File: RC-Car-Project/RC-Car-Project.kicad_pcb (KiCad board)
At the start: 2 copper layers, 80 x 120 mm, 118 parts, among them J1 Conn_01x02_Pin, J10 Conn_01x02, J2 Conn_01x02_Pin, J3 Conn_01x02_Pin, J4 Conn_01x02_Pin, J5 MCU_IF, J6 ANT_IF, J7 Conn_02x09_Odd_Even, J8 Conn_01x02, J9 Conn_01x02, Q1 BTN8982TA, Q2 BTN8982TA, Q3 2N7002E, Q4 2N7002E, Q5 BTN8982TA, Q6 BTN8982TA, Q7 2N7002E, SW1 SW_Push, U1 AT86RF215-ZU, U2 A6986F3V3TR, U3 ADC082S021CIMM/NOPB, U4 LMR16020PDDAR, U5 RFX2401C, U6 2450FB15A050E, U7 STM32H743VGTx, U8 INA229AQDGSRQ1, U9 SN74HC244PWR, Y1 Crystal

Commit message: Moved stuff around
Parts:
- moved SW1 75.9 mm to (59.1, 132.0)
- moved C10 75.9 mm to (74.9, 132.9)
- moved C11 75.9 mm to (74.9, 134.6)
- moved C14 75.9 mm to (86.1, 114.6)
- moved C15 75.9 mm to (86.1, 118.9)
- moved C2 75.9 mm to (86.1, 110.4)
- moved C22 75.9 mm to (92.6, 109.1)
- moved C23 75.9 mm to (92.6, 110.9)
- moved C37 75.9 mm to (92.6, 112.6)
- moved C39 75.9 mm to (86.1, 123.1)
- moved C43 75.9 mm to (92.6, 114.4)
- moved C44 75.9 mm to (92.6, 116.1)
- moved C45 75.9 mm to (92.6, 117.9)
- moved C46 75.9 mm to (86.1, 127.4)
- moved C47 75.9 mm to (86.1, 131.6)
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
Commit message: Candidate for layout #1?
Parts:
- moved U3 134.2 mm to (175.5, 116.0)
- moved Q4 126.9 mm to (172.9, 123.5)
- moved Q7 126.2 mm to (173.0, 136.5)
- moved Q3 126.1 mm to (173.0, 130.0)
- moved U1 105.8 mm to (138.5, 132.0)
- moved J6 101.4 mm to (116.2, 130.9)
- moved R15 98.3 mm to (129.0, 92.5)
- moved U6 96.9 mm to (131.9, 131.0)
- moved U5 94.9 mm to (124.5, 130.5), turned to 180 degrees
- moved U8 93.3 mm to (122.0, 96.5), turned to 90 degrees
- moved U7 90.4 mm to (155.5, 132.5), turned to -90 degrees
- moved L2 88.5 mm to (184.0, 108.0), turned to -90 degrees
- moved L1 83.5 mm to (171.5, 97.5), turned to 90 degrees
- moved Y1 81.0 mm to (156.0, 118.0)
- moved J9 80.3 mm to (183.5, 143.8), turned to 90 degrees
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
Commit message: Fixed Drivers
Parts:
- added R32: 10k, Resistor_SMD:R_0201_0603Metric, F.Cu at (93.2, 77.2)
- added R33: 10k, Resistor_SMD:R_0201_0603Metric, F.Cu at (93.2, 79.0)
- added R34: 10k, Resistor_SMD:R_0201_0603Metric, F.Cu at (93.2, 80.8)
- added R35: 10k, Resistor_SMD:R_0201_0603Metric, F.Cu at (93.2, 82.5)
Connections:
- J8 pad 1: /Connectors/LIGHTS1_POS -> +12V
- J9 pad 1: /Connectors/LIGHTS2_POS -> +12V
- Q1 pad 3: Net-(Q1-INH) -> +3V3
- Q2 pad 3: Net-(Q2-INH) -> +3V3
- Q3 pad 3: /MiscDriver/LIGHTS1_NEG -> /Connectors/LIGHTS1_NEG
- Q5 pad 3: Net-(Q5-INH) -> +3V3
- Q6 pad 3: Net-(Q6-INH) -> +3V3
- Q7 pad 3: /MiscDriver/LIGHTS2_NEG -> /Connectors/LIGHTS2_NEG
- R1 pad 1: /MiscDriver/MCU_LIGHTS1_CTRL -> /MCU/LIGHTS1_PWM
- R30 pad 1: /MiscDriver/MCU_LIGHTS2_CTRL -> /MCU/LIGHTS2_PWM
- U7 pad 23: /MCU/LEFT_EN1 -> /MCU/MOTOR_EN
- U7 pad 25: /MCU/LEFT_EN2 -> unconnected-(U7-PA3-Pad25)
- U7 pad 34: unconnected-(U7-PB0-Pad34) -> /MCU/LIGHTS2_PWM
- U7 pad 44: /MCU/LIGHTS_PWM -> /MCU/LIGHTS1_PWM
- U7 pad 60: /MCU/RIGHT_EN1 -> unconnected-(U7-PD13-Pad60)
- U7 pad 81: /MCU/RELAY_CTRL -> unconnected-(U7-PD0-Pad81)
- U7 pad 90: /MCU/RIGHT_EN2 -> unconnected-(U7-PB4-Pad90)
- U9 pad 1: GNDA -> /MCU/MOTOR_EN
- U9 pad 11: /MCU/LEFT_EN1 -> unconnected-(U9-2A1-Pad11)
- U9 pad 12: Net-(Q2-IN) -> Net-(Q6-IN)
- U9 pad 13: /MCU/LEFT_PWM1 -> unconnected-(U9-2A2-Pad13)
- U9 pad 14: Net-(Q2-INH) -> Net-(Q5-IN)
- U9 pad 15: /MCU/RIGHT_EN1 -> unconnected-(U9-2A3-Pad15)
- U9 pad 16: Net-(Q1-IN) -> Net-(Q2-IN)
- U9 pad 17: /MCU/RIGHT_PWM1 -> unconnected-(U9-2A4-Pad17)
- U9 pad 18: Net-(Q1-INH) -> Net-(Q1-IN)
- U9 pad 2: /MCU/LEFT_EN2 -> /MCU/LEFT_PWM1
- U9 pad 3: Net-(Q6-IN) -> unconnected-(U9-2Y4-Pad3)
- U9 pad 4: /MCU/LEFT_PWM2 -> /MCU/RIGHT_PWM1
- U9 pad 5: Net-(Q6-INH) -> unconnected-(U9-2Y3-Pad5)
- U9 pad 6: /MCU/RIGHT_EN2 -> /MCU/LEFT_PWM2
- U9 pad 7: Net-(Q5-IN) -> unconnected-(U9-2Y2-Pad7)
- U9 pad 9: Net-(Q5-INH) -> unconnected-(U9-2Y1-Pad9)

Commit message: Fixed Annotations
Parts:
- C1: renamed from C39; footprint Capacitor_SMD:C_1210_3225Metric -> Capacitor_SMD:C_0603_1608Metric
- C10: renamed from C46; footprint Capacitor_SMD:C_1210_3225Metric -> Capacitor_SMD:C_0603_1608Metric
- C11: renamed from C47; footprint Capacitor_SMD:C_1210_3225Metric -> Capacitor_SMD:C_0603_1608Metric
- C12: renamed from C48; footprint Capacitor_SMD:C_0201_0603Metric -> Capacitor_SMD:C_0603_1608Metric
- C13: renamed from C23; footprint Capacitor_SMD:C_0201_0603Metric -> Capacitor_SMD:C_0603_1608Metric
- C14: renamed from C15; footprint Capacitor_SMD:C_1210_3225Metric -> Capacitor_SMD:C_0603_1608Metric
- C15: renamed from C2; footprint Capacitor_SMD:C_1210_3225Metric -> Capacitor_SMD:C_0603_1608Metric
- C16: footprint Capacitor_SMD:C_0201_0603Metric -> Capacitor_SMD:C_0603_1608Metric
- C17: renamed from C14; footprint Capacitor_SMD:C_1210_3225Metric -> Capacitor_SMD:C_0603_1608Metric
- C18: renamed from C1; footprint Capacitor_SMD:C_0201_0603Metric -> Capacitor_SMD:C_0603_1608Metric
- C19: renamed from C22; footprint Capacitor_SMD:C_0201_0603Metric -> Capacitor_SMD:C_0603_1608Metric
- C2: renamed from C43; footprint Capacitor_SMD:C_0201_0603Metric -> Capacitor_SMD:C_0603_1608Metric
- C20: renamed from C35; footprint Capacitor_SMD:C_0201_0603Metric -> Capacitor_SMD:C_0603_1608Metric
- C21: renamed from C36; footprint Capacitor_SMD:C_0201_0603Metric -> Capacitor_SMD:C_0603_1608Metric
- C22: renamed from C34; footprint Capacitor_SMD:C_0201_0603Metric -> Capacitor_SMD:C_0603_1608Metric
- C23: renamed from C21; footprint Capacitor_SMD:C_0201_0603Metric -> Capacitor_SMD:C_0603_1608Metric
- C24: renamed from C40; footprint Capacitor_SMD:C_0201_0603Metric -> Capacitor_SMD:C_0603_1608Metric
- C25: renamed from C7; footprint Capacitor_SMD:C_0201_0603Metric -> Capacitor_SMD:C_0603_1608Metric
- C26: renamed from C8; footprint Capacitor_SMD:C_0201_0603Metric -> Capacitor_SMD:C_0603_1608Metric
- C27: renamed from C9; footprint Capacitor_SMD:C_0201_0603Metric -> Capacitor_SMD:C_0603_1608Metric
- C28: renamed from C10; footprint Capacitor_SMD:C_0201_0603Metric -> Capacitor_SMD:C_0603_1608Metric
- C29: renamed from C11; footprint Capacitor_SMD:C_0201_0603Metric -> Capacitor_SMD:C_0603_1608Metric
- C3: renamed from C44; footprint Capacitor_SMD:C_0201_0603Metric -> Capacitor_SMD:C_0603_1608Metric
- C30: renamed from C12; footprint Capacitor_SMD:C_0201_0603Metric -> Capacitor_SMD:C_0603_1608Metric
- C31: renamed from C24; footprint Capacitor_SMD:C_0201_0603Metric -> Capacitor_SMD:C_0603_1608Metric
- C32: renamed from C25; footprint Capacitor_SMD:C_0201_0603Metric -> Capacitor_SMD:C_0603_1608Metric
- C33: renamed from C26; footprint Capacitor_SMD:C_0201_0603Metric -> Capacitor_SMD:C_0603_1608Metric
- C34: renamed from C27; footprint Capacitor_SMD:C_0201_0603Metric -> Capacitor_SMD:C_0603_1608Metric
- C35: renamed from C28; footprint Capacitor_SMD:C_0201_0603Metric -> Capacitor_SMD:C_0603_1608Metric
- C36: renamed from C29; footprint Capacitor_SMD:C_0201_0603Metric -> Capacitor_SMD:C_0603_1608Metric
- C37: renamed from C30; footprint Capacitor_SMD:C_0201_0603Metric -> Capacitor_SMD:C_0603_1608Metric
- C38: renamed from C31; footprint Capacitor_SMD:C_0201_0603Metric -> Capacitor_SMD:C_0603_1608Metric
- C39: renamed from C32; footprint Capacitor_SMD:C_0201_0603Metric -> Capacitor_SMD:C_0603_1608Metric
- C4: renamed from C17; footprint Capacitor_SMD:C_0201_0603Metric -> Capacitor_SMD:C_0603_1608Metric
- C40: renamed from C33; footprint Capacitor_SMD:C_0201_0603Metric -> Capacitor_SMD:C_0603_1608Metric
- C41: renamed from C3; footprint Capacitor_SMD:C_0201_0603Metric -> Capacitor_SMD:C_0603_1608Metric
- C42: renamed from C4; footprint Capacitor_SMD:C_0201_0603Metric -> Capacitor_SMD:C_0603_1608Metric
- C43: renamed from C38; footprint Capacitor_SMD:C_0201_0603Metric -> Capacitor_SMD:C_0603_1608Metric
- C44: renamed from C13; footprint Capacitor_SMD:C_0201_0603Metric -> Capacitor_SMD:C_0603_1608Metric
- C45: renamed from C6; footprint Capacitor_SMD:C_0201_0603Metric -> Capacitor_SMD:C_0603_1608Metric
- C46: renamed from C5; footprint Capacitor_SMD:C_0201_0603Metric -> Capacitor_SMD:C_0603_1608Metric
- C47: renamed from C41; footprint Capacitor_SMD:C_0201_0603Metric -> Capacitor_SMD:C_0603_1608Metric
- C48: renamed from C42; footprint Capacitor_SMD:C_0201_0603Metric -> Capacitor_SMD:C_0603_1608Metric
- C5: renamed from C18; footprint Capacitor_SMD:C_0201_0603Metric -> Capacitor_SMD:C_0603_1608Metric
- C6: renamed from C20; footprint Capacitor_SMD:C_0201_0603Metric -> Capacitor_SMD:C_0603_1608Metric
- C7: renamed from C37; footprint Capacitor_SMD:C_0201_0603Metric -> Capacitor_SMD:C_0603_1608Metric
- C8: renamed from C45; footprint Capacitor_SMD:C_0201_0603Metric -> Capacitor_SMD:C_0603_1608Metric
- C9: renamed from C19; footprint Capacitor_SMD:C_0201_0603Metric -> Capacitor_SMD:C_0603_1608Metric
- D1, D2: footprint LED_SMD:LED_0201_0603Metric -> LED_SMD:LED_0603_1608Metric
- R1: renamed from R13; footprint Resistor_SMD:R_0201_0603Metric -> Resistor_SMD:R_0603_1608Metric
- R10: renamed from R29; footprint Resistor_SMD:R_0201_0603Metric -> Resistor_SMD:R_0603_1608Metric
- R11: renamed from R8; footprint Resistor_SMD:R_0201_0603Metric -> Resistor_SMD:R_0603_1608Metric
- R12: renamed from R9; footprint Resistor_SMD:R_0201_0603Metric -> Resistor_SMD:R_0603_1608Metric
- R13: renamed from R10; footprint Resistor_SMD:R_0201_0603Metric -> Resistor_SMD:R_0603_1608Metric
- R14: renamed from R12; footprint Resistor_SMD:R_0201_0603Metric -> Resistor_SMD:R_0603_1608Metric
- R15: renamed from R11; footprint Resistor_SMD:R_0201_0603Metric -> Resistor_SMD:R_0603_1608Metric
- R16: renamed from R24; footprint Resistor_SMD:R_0201_0603Metric -> Resistor_SMD:R_0603_1608Metric
- R17: renamed from R4; footprint Resistor_SMD:R_0201_0603Metric -> Resistor_SMD:R_0603_1608Metric
- R18: renamed from R2; footprint Resistor_SMD:R_0201_0603Metric -> Resistor_SMD:R_0603_1608Metric
- R19: renamed from R3; footprint Resistor_SMD:R_0201_0603Metric -> Resistor_SMD:R_0603_1608Metric
- R2: renamed from R14; footprint Resistor_SMD:R_0201_0603Metric -> Resistor_SMD:R_0603_1608Metric
- R21: renamed from R23; footprint Resistor_SMD:R_0201_0603Metric -> Resistor_SMD:R_0603_1608Metric
- R22: renamed from R35; footprint Resistor_SMD:R_0201_0603Metric -> Resistor_SMD:R_0603_1608Metric
- R23: renamed from R32; footprint Resistor_SMD:R_0201_0603Metric -> Resistor_SMD:R_0603_1608Metric
- R24: renamed from R33; footprint Resistor_SMD:R_0201_0603Metric -> Resistor_SMD:R_0603_1608Metric
- R25: renamed from R34; footprint Resistor_SMD:R_0201_0603Metric -> Resistor_SMD:R_0603_1608Metric
- R26: renamed from R6; footprint Resistor_SMD:R_0201_0603Metric -> Resistor_SMD:R_0603_1608Metric
- R27: renamed from R5; footprint Resistor_SMD:R_0201_0603Metric -> Resistor_SMD:R_0603_1608Metric
- R28: renamed from R17; footprint Resistor_SMD:R_0201_0603Metric -> Resistor_SMD:R_0603_1608Metric
- R29: renamed from R18; footprint Resistor_SMD:R_0201_0603Metric -> Resistor_SMD:R_0603_1608Metric
- R3: renamed from R26; footprint Resistor_SMD:R_0201_0603Metric -> Resistor_SMD:R_0603_1608Metric
- R30: renamed from R1; footprint Resistor_SMD:R_0201_0603Metric -> Resistor_SMD:R_0603_1608Metric
- R31: renamed from R30; footprint Resistor_SMD:R_0201_0603Metric -> Resistor_SMD:R_0603_1608Metric
- R32: renamed from R16; footprint Resistor_SMD:R_0201_0603Metric -> Resistor_SMD:R_0603_1608Metric
- R33: renamed from R31; footprint Resistor_SMD:R_0201_0603Metric -> Resistor_SMD:R_0603_1608Metric
- R4: renamed from R25; footprint Resistor_SMD:R_0201_0603Metric -> Resistor_SMD:R_0603_1608Metric
- R5: renamed from R27; footprint Resistor_SMD:R_0201_0603Metric -> Resistor_SMD:R_0603_1608Metric
- R6: renamed from R21; footprint Resistor_SMD:R_0201_0603Metric -> Resistor_SMD:R_0603_1608Metric
- R7: footprint Resistor_SMD:R_0201_0603Metric -> Resistor_SMD:R_0603_1608Metric
- R8: renamed from R22; footprint Resistor_SMD:R_0201_0603Metric -> Resistor_SMD:R_0603_1608Metric
- R9: renamed from R28; footprint Resistor_SMD:R_0201_0603Metric -> Resistor_SMD:R_0603_1608Metric
- moved C48 100.6 mm to (184.2, 81.3), turned to -90 degrees
- moved R29 96.2 mm to (182.6, 81.3), turned to -90 degrees
- moved C47 90.0 mm to (171.7, 81.3), turned to -90 degrees
- moved R22 85.7 mm to (178.8, 81.3), turned to 90 degrees
- moved R28 85.5 mm to (170.0, 81.3), turned to -90 degrees
- moved R25 73.0 mm to (166.1, 81.3), turned to 90 degrees
- moved C44 72.5 mm to (145.3, 90.2), turned to -90 degrees
- moved C45 59.3 mm to (134.1, 81.3), turned to -90 degrees
- moved R26 55.8 mm to (132.6, 81.3), turned to -90 degrees
- moved C46 51.9 mm to (121.9, 81.3), turned to -90 degrees
- moved R27 46.7 mm to (120.4, 81.3), turned to -90 degrees
- moved R23 35.7 mm to (128.7, 81.3), turned to 90 degrees
- moved C16 32.6 mm to (65.8, 89.2)
- moved C18 32.6 mm to (65.8, 87.5)
- moved C4 32.6 mm to (65.8, 91.0)
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- renumbered J6 to J10, J8 to J6, J9 to J7, J10 to J8, J7 to J9, L2 to L1, L1 to L2, Q5 to Q3, Q6 to Q4, Q3 to Q5, Q7 to Q6, R15 to R20, U4 to U1, U7 to U3, U1 to U4, U6 to U5, U5 to U6, U8 to U7, U3 to U8
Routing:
- net Net-(Q3-SR): track 0.00 -> 5.62 mm
- net Net-(Q4-SR): track 0.00 -> 5.49 mm
- net Net-(Q2-SR): track 0.00 -> 5.48 mm
- net Net-(Q1-SR): track 0.00 -> 5.43 mm
- net Net-(Q3-IN): track 0.00 -> 3.93 mm
- net Net-(Q4-IN): track 0.00 -> 3.91 mm
- net Net-(Q2-IN): track 0.00 -> 3.90 mm
- net Net-(Q1-IN): track 0.00 -> 3.89 mm

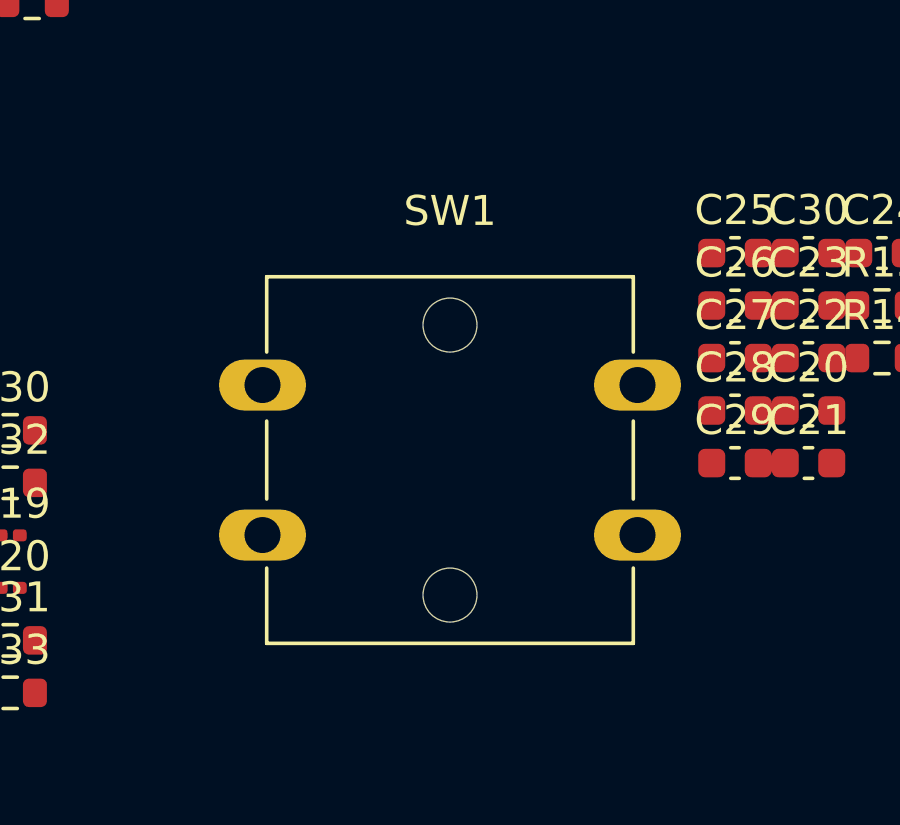
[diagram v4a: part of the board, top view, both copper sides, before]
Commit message: Change button footprint
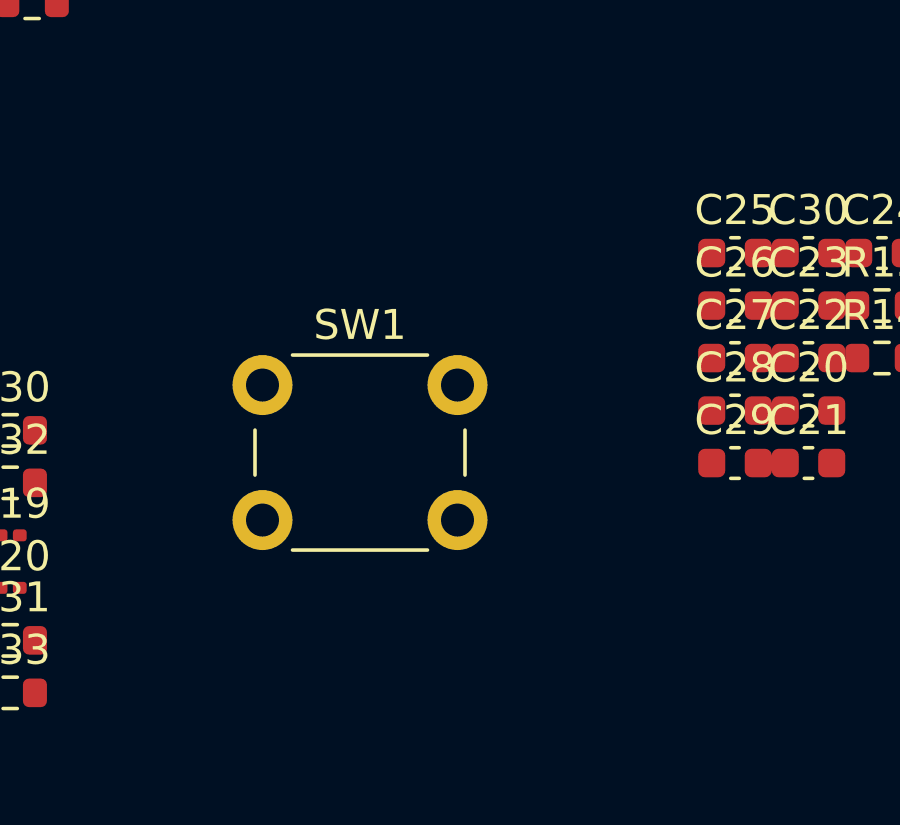
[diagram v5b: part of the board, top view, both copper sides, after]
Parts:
- SW1: footprint Button_Switch_THT:SW_SPST_Omron_B3F-40xx -> Button_Switch_THT:SW_PUSH_6mm
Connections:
- U3 pad 72: unconnected-(U3-PA13-Pad72) -> /Connectors/SWDIO
- U3 pad 77: /Connectors/SWDIO -> unconnected-(U3-PA15-Pad77)

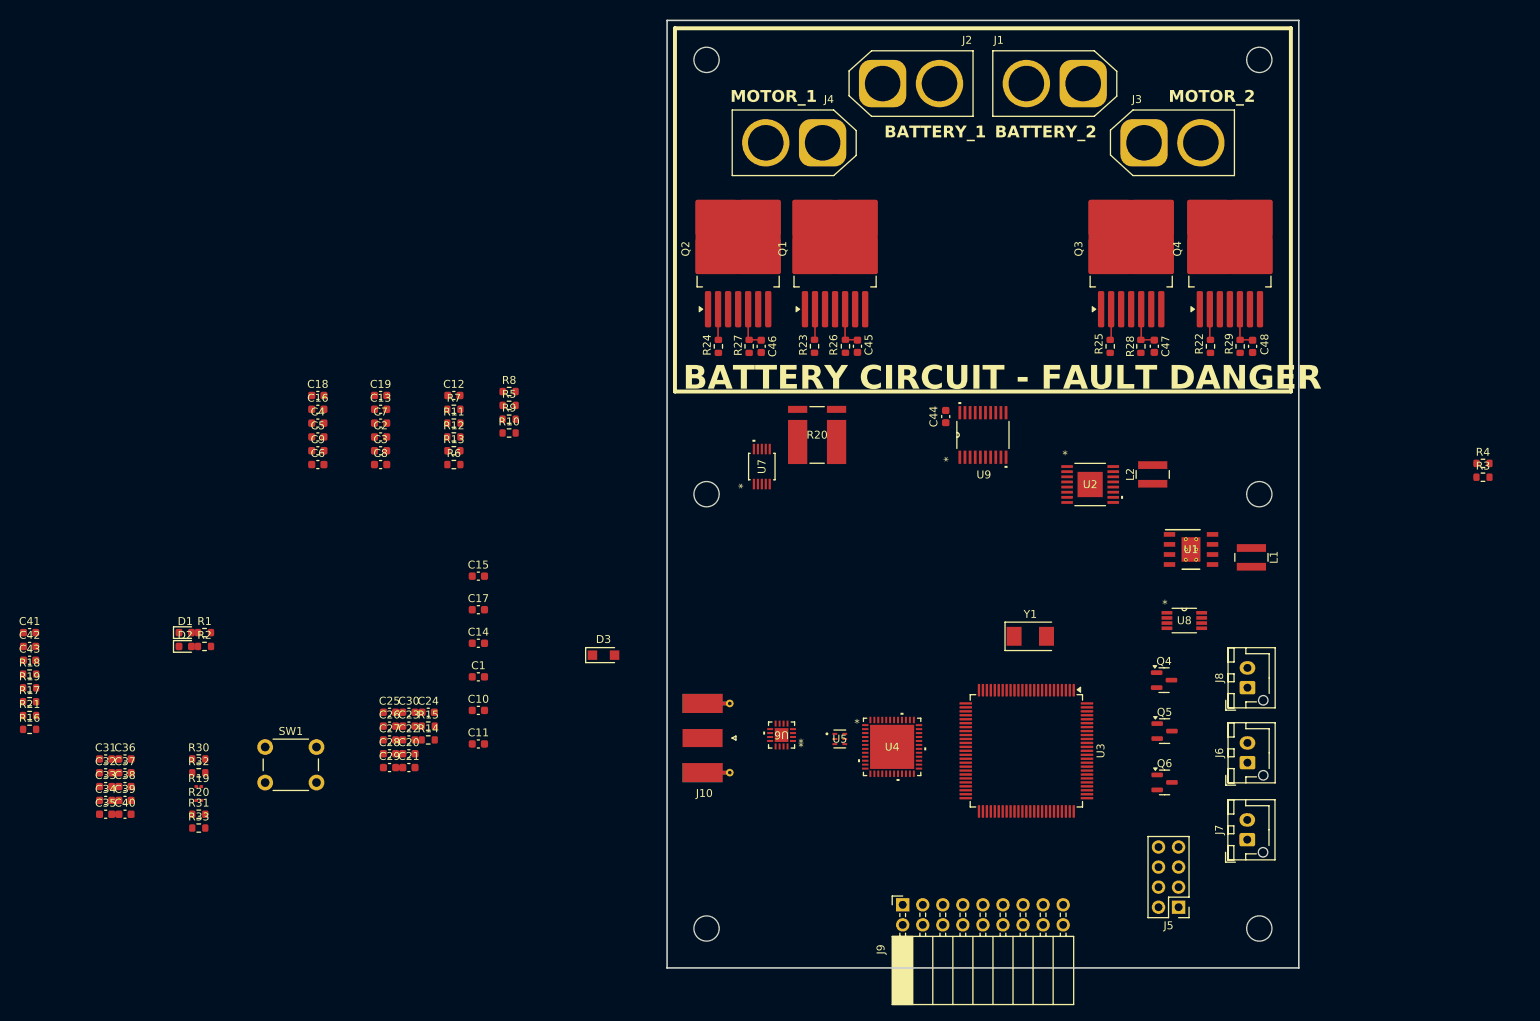
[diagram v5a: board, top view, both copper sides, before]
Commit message: Add RF filter + another thermo header + layout everything
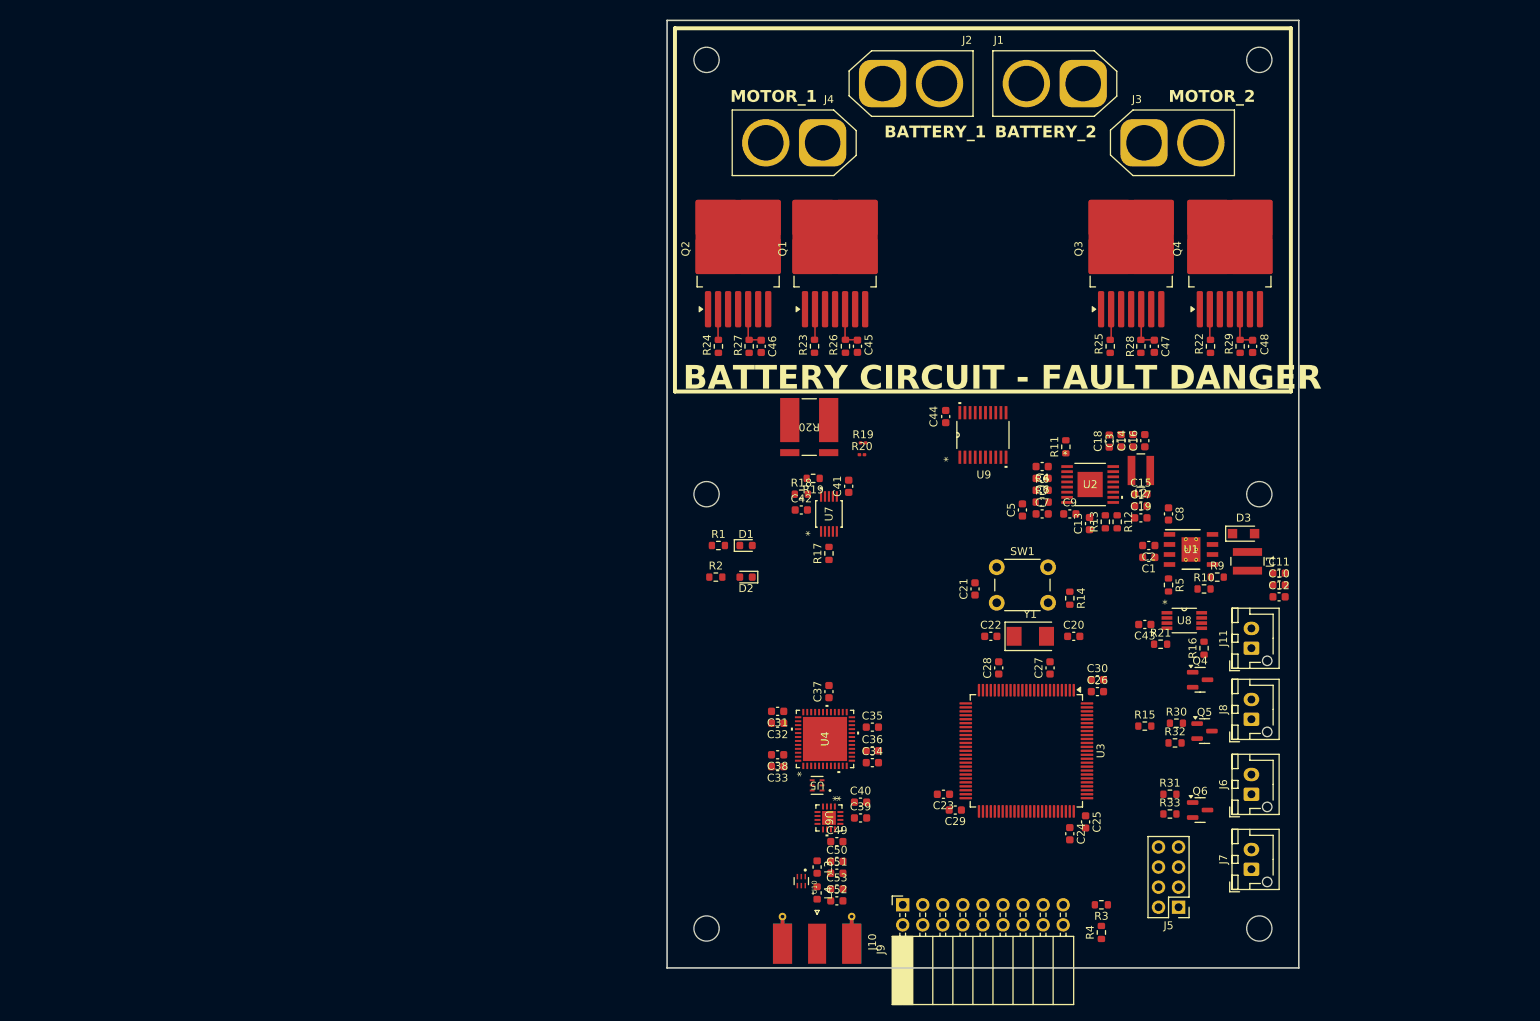
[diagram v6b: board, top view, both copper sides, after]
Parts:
- removed R8: 56kohm, Resistor_SMD:R_0603_1608Metric
- added C49: 0.3pF, Capacitor_SMD:C_0603_1608Metric, F.Cu at (131.5, 144.0)
- added C50: 1.5pF, Capacitor_SMD:C_0603_1608Metric, F.Cu at (131.5, 146.5)
- added C51: 1.5pF, Capacitor_SMD:C_0603_1608Metric, F.Cu at (131.5, 148.0)
- added C52: 1.5pF, Capacitor_SMD:C_0603_1608Metric, F.Cu at (131.5, 151.5)
- added C53: 1.5pF, Capacitor_SMD:C_0603_1608Metric, F.Cu at (131.5, 150.0)
- added J11: Conn_01x02, Connector_JST:JST_XH_B2B-XH-AM_1x02_P2.50mm_Vertical, F.Cu at (184.0, 119.5)
- added L3: 2.4nH, Inductor_SMD:L_0603_1608Metric, F.Cu at (129.0, 147.2)
- added L4: 2.4nH, Inductor_SMD:L_0603_1608Metric, F.Cu at (129.0, 150.5)
- added U10: 2450LP14A0100001T, footprints:ICCAF50P160X80X70-6N, F.Cu at (127.0, 149.0)
- moved R16 149.1 mm to (178.0, 119.5), turned to 90 degrees
- moved R21 143.5 mm to (172.5, 119.0)
- moved C43 141.3 mm to (170.5, 116.5), turned to 180 degrees
- moved R30 123.9 mm to (174.5, 129.0)
- moved R32 123.7 mm to (174.3, 131.5)
- moved R31 123.0 mm to (173.7, 138.0)
- moved R33 123.0 mm to (173.7, 140.5)
- moved C12 107.6 mm to (187.5, 113.0)
- moved C41 105.4 mm to (133.0, 99.0), turned to 90 degrees
- moved C16 104.8 mm to (170.5, 93.2), turned to 90 degrees
- moved C11 103.7 mm to (187.5, 110.0)
- moved R17 103.0 mm to (130.5, 107.5), turned to 90 degrees
- moved R19 102.7 mm to (128.5, 98.0), turned to 180 degrees
- moved C10 102.6 mm to (187.5, 111.5)
- moved C18 100.4 mm to (166.0, 93.3), turned to 90 degrees
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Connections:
- J8 pad 1: /Connectors/THERMO1 -> +3V3
- J8 pad 2: /Connectors/THERMO2 -> /Connectors/THERMO1_NEG
- R16 pad 2: /Connectors/THERMO2 -> /Connectors/THERMO2_NEG
- R21 pad 2: /Connectors/THERMO1 -> /Connectors/THERMO1_NEG
- U6 pad 10: /Connectors/RF_ANT -> Net-(U10-IN)
- U8 pad 4: /Connectors/THERMO1 -> /Connectors/THERMO1_NEG
- U8 pad 5: /Connectors/THERMO2 -> /Connectors/THERMO2_NEG
